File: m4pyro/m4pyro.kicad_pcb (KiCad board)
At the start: 2 copper layers, 140 parts, among them IC1 STM32F405RxTx, IC10 LTC4151, IC2 TPS62133, IC3 MCP2562, IC4 TPS62153, IC5 ADP2389, IC6 LTC4151, IC7 ADP2389, IC8 LTC4151, IC9 ADP2389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

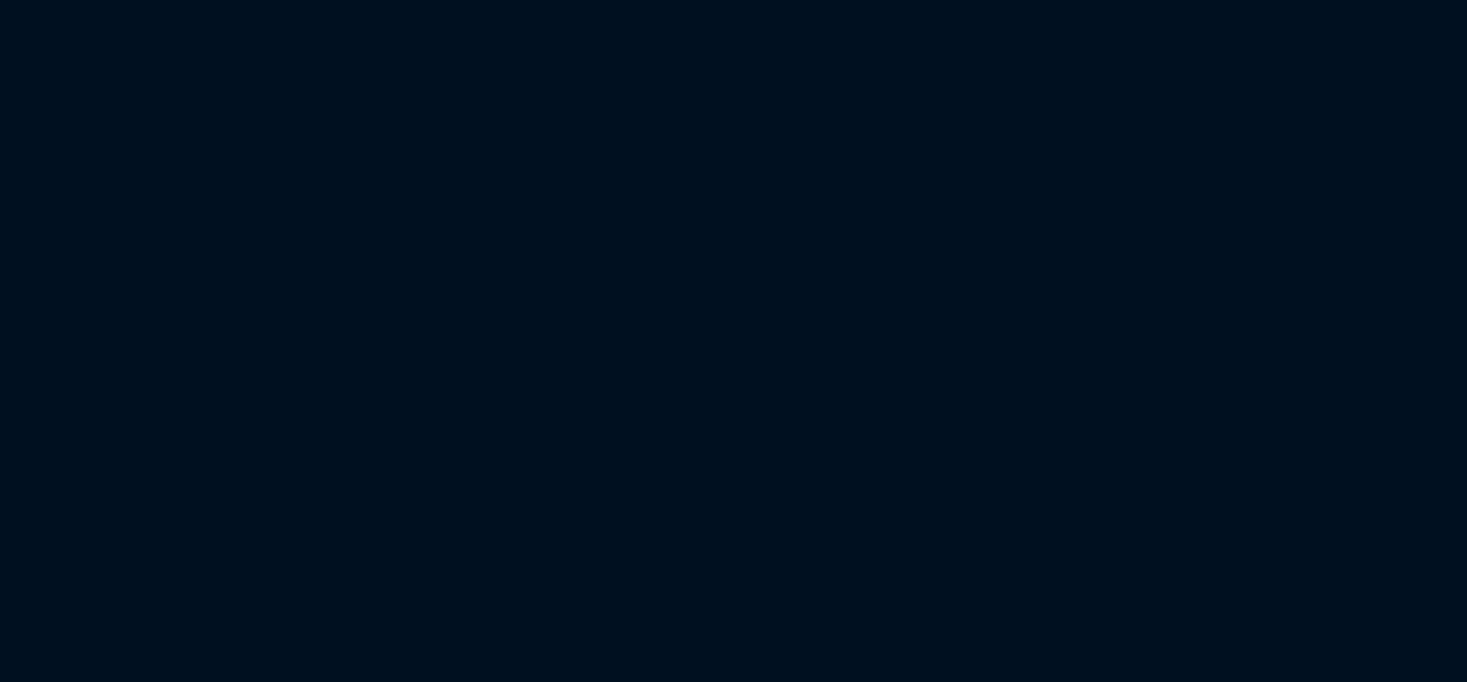
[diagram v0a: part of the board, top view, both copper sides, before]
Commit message: pyro schematic almost done
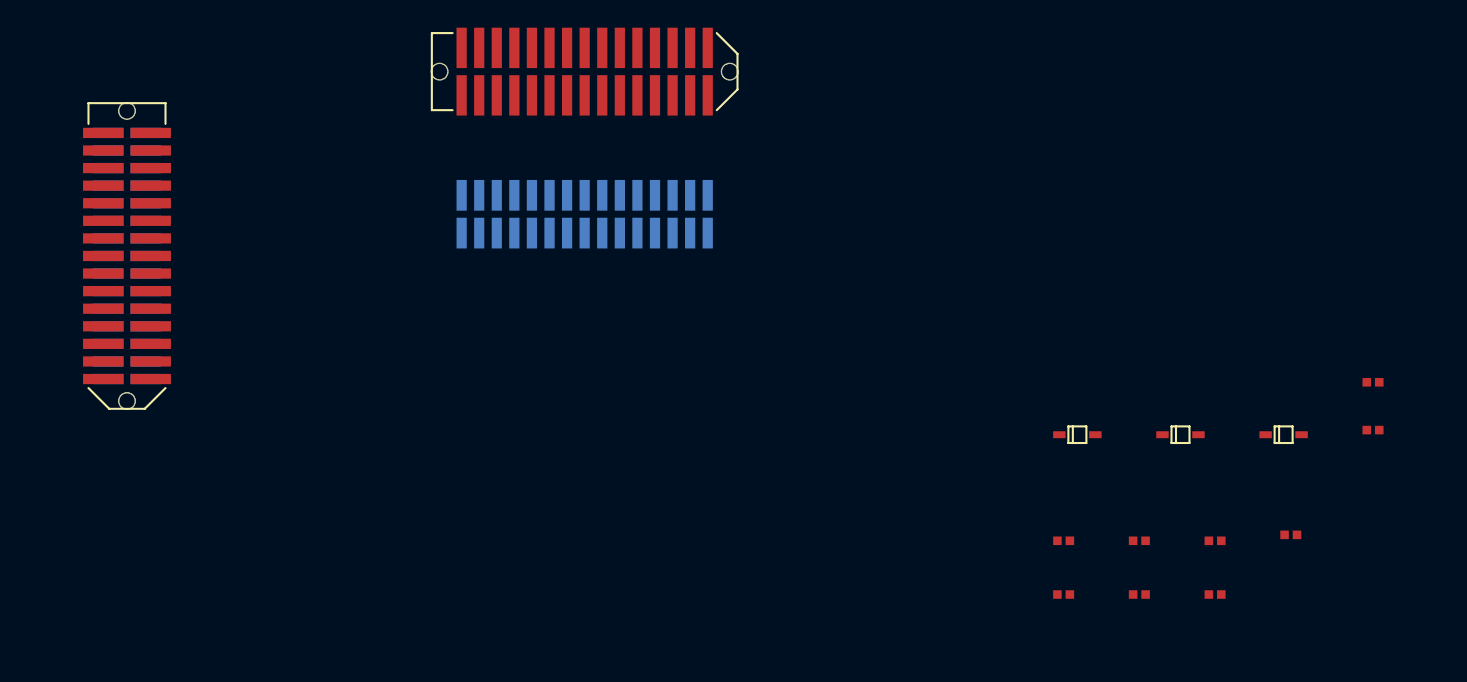
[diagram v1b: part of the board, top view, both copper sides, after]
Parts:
- added C48: 100n, agg:0402, F.Cu at (183.7, 46.2)
- added C49: 100n, agg:0402, F.Cu at (189.1, 46.2)
- added C50: 100n, agg:0402, F.Cu at (194.6, 46.2)
- added D12: PMEG3005AEA, agg:SOD-323, F.Cu at (184.7, 38.5)
- added D13: PMEG3005AEA, agg:SOD-323, F.Cu at (192.1, 38.5)
- added D14: PMEG3005AEA, agg:SOD-323, F.Cu at (199.6, 38.5)
- added J1: WEST TOP, agg:TFML-115-02-L-D-LC, F.Cu at (116.0, 25.6)
- added J2: WEST BOT, agg:SFML-115-02-L-D, B.Cu at (116.0, 25.6)
- added J3: EAST TOP, agg:TFML-115-02-L-D-LC, F.Cu at (149.1, 12.3)
- added J4: EAST BOT, agg:SFML-115-02-L-D, B.Cu at (149.1, 22.6)
- added R58: 1k, agg:0402, F.Cu at (183.7, 50.1)
- added R59: 1k, agg:0402, F.Cu at (189.1, 50.1)
- added R60: 1k, agg:0402, F.Cu at (206.0, 34.7)
- added R61: 10k, agg:0402, F.Cu at (194.6, 50.1)
- added R62: 10k, agg:0402, F.Cu at (206.0, 38.2)
- added R63: 10k, agg:0402, F.Cu at (200.1, 45.7)
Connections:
- IC1 pad 50: (no net) -> /JTDI
- IC1 pad 55: (no net) -> /JTDO
- IC3 pad 6: (no net) -> /CAN-
- IC3 pad 7: (no net) -> /CAN+

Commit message: started pyro pcb
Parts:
- added X2: HOLE, agg:M3_MOUNT, F.Cu at (57.5, 84.0)
- added X3: HOLE, agg:M3_MOUNT, F.Cu at (57.5, 116.0)
- added X4: HOLE, agg:M3_MOUNT, F.Cu at (142.5, 84.0)
- added X5: HOLE, agg:M3_MOUNT, F.Cu at (142.5, 116.0)
- L3, L4, L5: footprint agg:WE-HCC-1090 -> agg:WE-HCC-1090
- moved L4 204.8 mm to (273.5, 92.0), turned to 0 degrees
- moved IC9 181.4 mm to (232.9, 24.7)
- moved L5 160.4 mm to (274.4, 102.9)
- moved L3 154.6 mm to (188.6, 9.70)
- moved IC5 144.5 mm to (184.4, 19.2)
- moved IC7 139.3 mm to (200.0, 62.8)
- moved R44 131.9 mm to (167.2, 14.1)
- moved C30 117.6 mm to (193.0, 21.1)
- moved R46 115.9 mm to (193.2, 25.8)
- moved C40 109.4 mm to (185.5, 26.3)
- moved R45 104.3 mm to (193.2, 24.2)
- moved C27 97.4 mm to (191.6, 17.2)
- moved Q5 97.0 mm to (178.4, 76.4)
- moved R53 94.9 mm to (233.3, 68.8)
- moved J1 94.6 mm to (57.5, 100.0)
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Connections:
- IC1 pad 10: (no net) -> /V3_CONT
- IC1 pad 14: /LED_RED -> /CH1_CONT
- IC1 pad 15: /LED_YLW -> /CH2_CONT
- IC1 pad 16: /LED_GRN -> /CH3_CONT
- IC1 pad 17: (no net) -> /CH4_CONT
- IC1 pad 2: (no net) -> /LED_RED
- IC1 pad 20: /SI_DIV -> /CH5_CONT
- IC1 pad 21: /BUS_DIV -> /CH6_CONT
- IC1 pad 22: (no net) -> /CH7_CONT
- IC1 pad 23: (no net) -> /CH8_CONT
- IC1 pad 26: (no net) -> /SI_DIV
- IC1 pad 27: (no net) -> /BUS_DIV
- IC1 pad 29: (no net) -> /SCL
- IC1 pad 3: (no net) -> /LED_YLW
- IC1 pad 30: (no net) -> /SDA
- IC1 pad 4: (no net) -> /LED_GRN
- IC1 pad 42: (no net) -> /UART_TX
- IC1 pad 43: /1A_EN -> /UART_RX
- IC1 pad 44: (no net) -> /1A_EN
- IC1 pad 51: (no net) -> /V1_FIRE
- IC1 pad 52: (no net) -> /V2_FIRE
- IC1 pad 53: (no net) -> /V3_FIRE
- IC1 pad 8: (no net) -> /V1_CONT
- IC1 pad 9: (no net) -> /V2_CONT
- IC5 pad 28: (no net) -> /V1_FIRE
- IC7 pad 28: (no net) -> /V2_FIRE
- IC9 pad 28: (no net) -> /V3_FIRE
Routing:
- net GND: track 0.00 -> 101.9 mm, vias 0 -> 16
- net 3v3: track 0.00 -> 16.3 mm, vias 0 -> 2
- net /UART_RX: track 0.00 -> 3.32 mm, vias 0 -> 1
- net /3v3_AUX1: track 0.00 -> 3.32 mm, vias 0 -> 1
- net /RSVD8: track 0.00 -> 3.32 mm, vias 0 -> 1
- net /5v_RADIO: track 0.00 -> 3.32 mm, vias 0 -> 1
- net /RSVD4: track 0.00 -> 3.30 mm, vias 0 -> 1
- net /5v_CAN: track 0.00 -> 3.30 mm, vias 0 -> 1
- net /RSVD11: track 0.00 -> 3.30 mm, vias 0 -> 1
- net /PYRO6: track 0.00 -> 3.30 mm, vias 0 -> 1
- net /PYRO5: track 0.00 -> 3.30 mm, vias 0 -> 1
- net /RSVD12: track 0.00 -> 3.28 mm, vias 0 -> 1
- net /PYRO4: track 0.00 -> 3.28 mm, vias 0 -> 1
- net /PYRO3: track 0.00 -> 3.28 mm, vias 0 -> 1
- net /5v_CAM2: track 0.00 -> 3.28 mm, vias 0 -> 1
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- removed copper zone on F.Cu, net Net-(C37-Pad2)
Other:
- board outline added: 100 x 50 mm
- net class Default: clearance 0.2 -> 0.15; trace_width 0.25 -> 0.2; via_dia 0.8 -> 0.6
- rule trace_clearance: 0.2 -> 0.15
- rule via_min_size: 0.4 -> 0.6

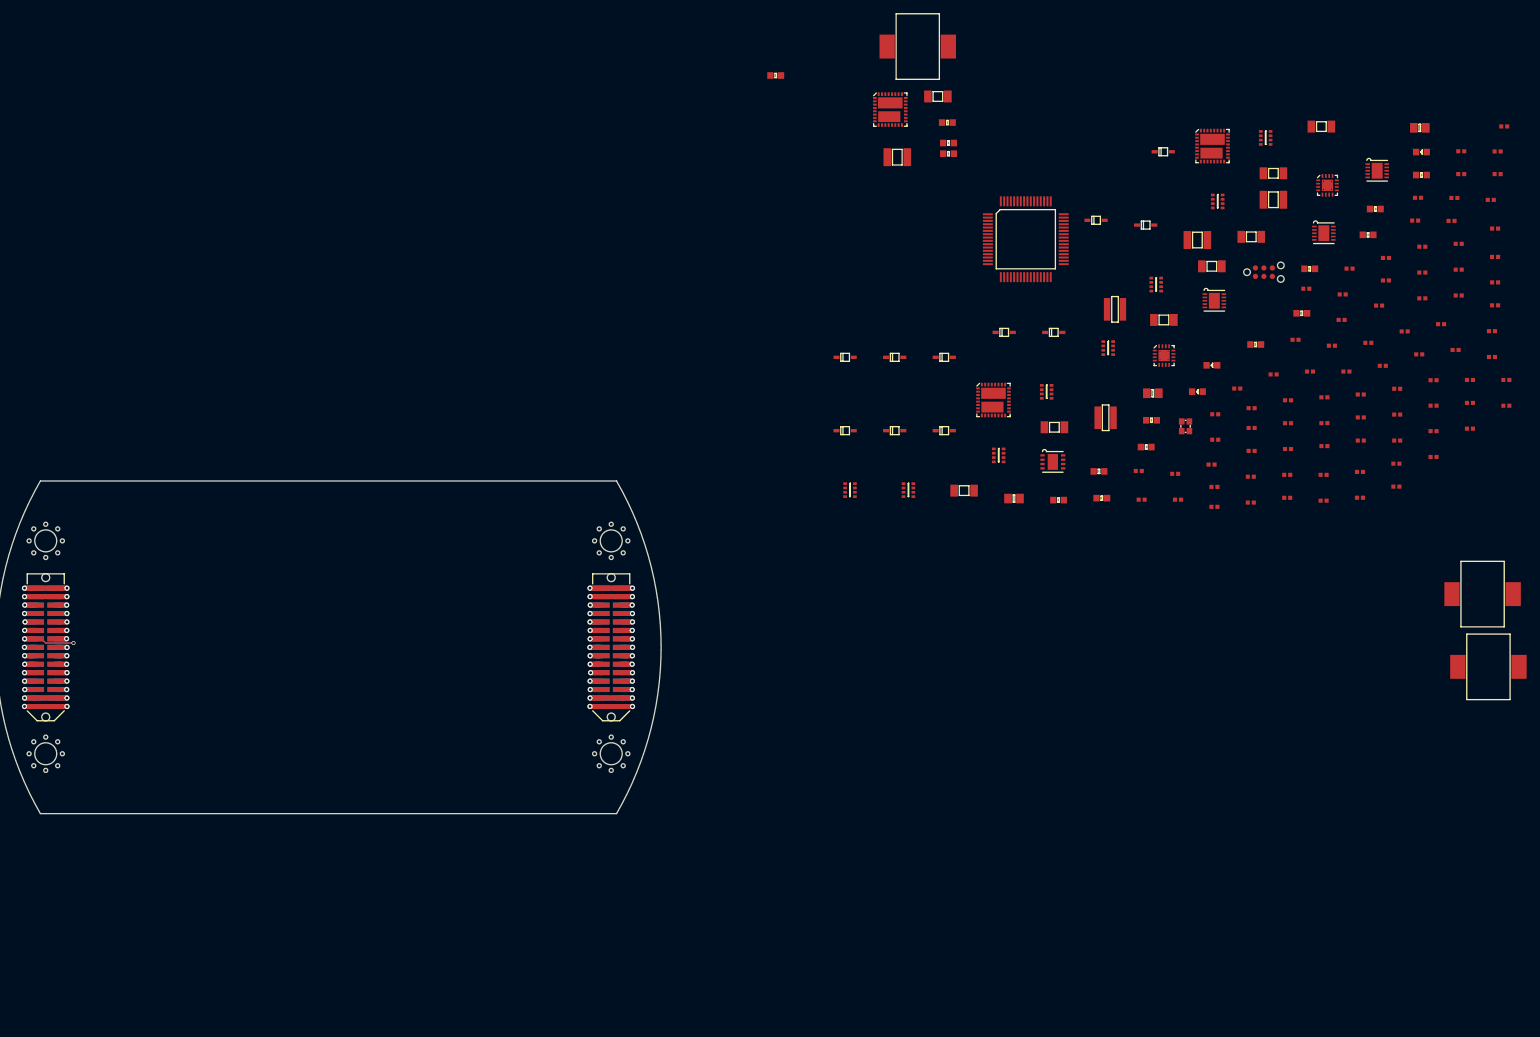
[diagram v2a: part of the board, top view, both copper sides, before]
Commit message: laying out pyro valve components
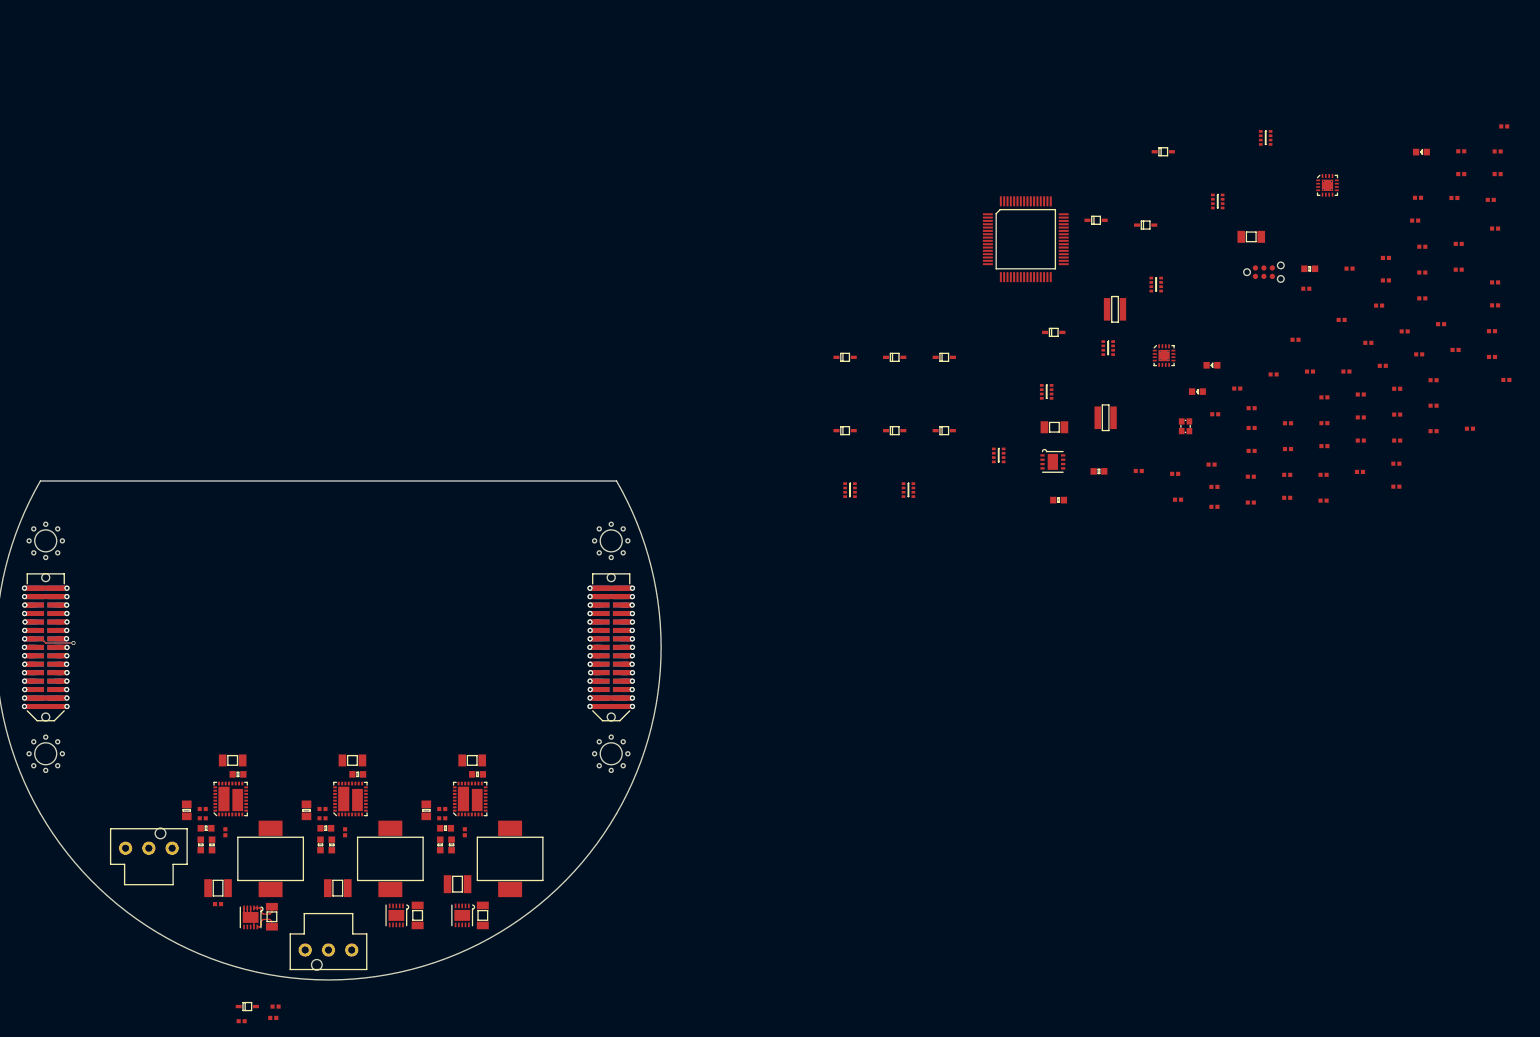
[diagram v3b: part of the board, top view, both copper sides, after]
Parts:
- added J5: SUPPLY, agg:ultra-fit-01x03, F.Cu at (73.0, 130.2)
- added J6: VALVES, agg:ultra-fit-01x03, F.Cu at (100.0, 145.5)
- moved R43 211.2 mm to (81.1, 124.3)
- moved C29 207.6 mm to (83.4, 138.6)
- moved C28 202.2 mm to (84.5, 127.8), turned to 90 degrees
- moved R61 201.2 mm to (92.0, 154.0)
- moved C39 196.3 mm to (96.7, 124.5), turned to 270 degrees
- moved C31 192.8 mm to (81.1, 125.7)
- moved C48 192.8 mm to (87.0, 156.2)
- moved C33 189.4 mm to (83.4, 136.2)
- moved C35 182.2 mm to (102.5, 127.8), turned to 90 degrees
- moved R49 180.3 mm to (99.6, 127.2), turned to 180 degrees
- moved R58 178.6 mm to (91.7, 155.7)
- moved IC10 177.3 mm to (120.1, 140.3), turned to 270 degrees
- moved R54 176.5 mm to (117.6, 127.2), turned to 180 degrees
- moved C45 176.3 mm to (117.1, 125.7)
- moved IC8 173.1 mm to (110.2, 140.3), turned to 270 degrees
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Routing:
- net GND: track 101.9 -> 108.6 mm
- net /V_1_SUPPLY: track 0.00 -> 4.24 mm
- net /VALVE_1: track 0.00 -> 3.94 mm
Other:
- board size 100 x 50 mm -> 100 x 75 mm

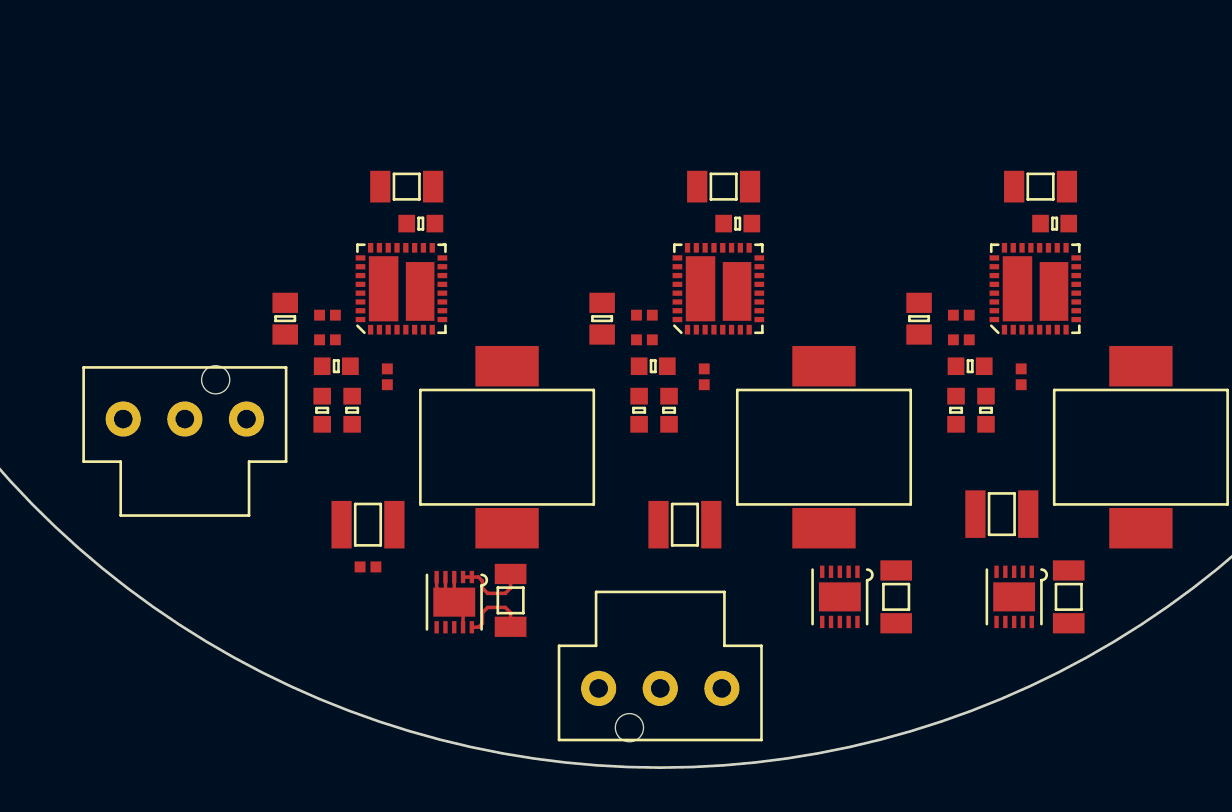
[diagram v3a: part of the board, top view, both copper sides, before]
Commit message: added pcb template
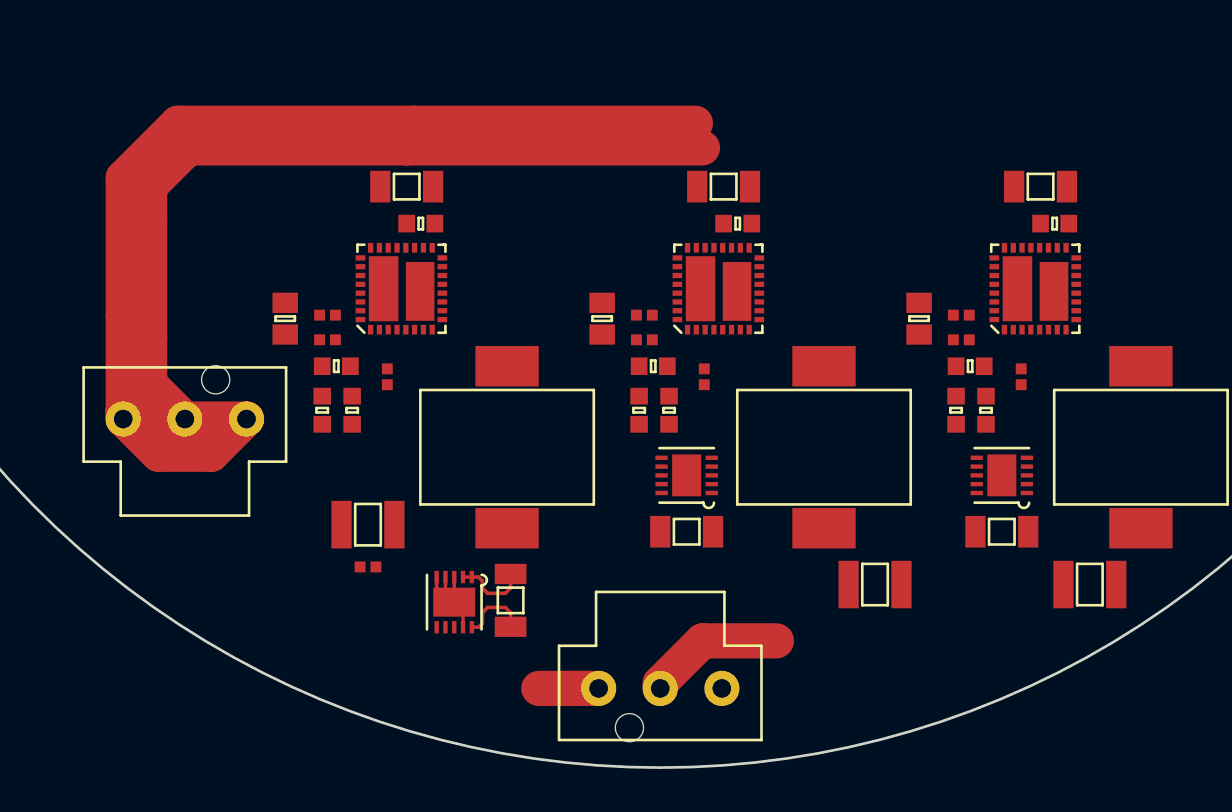
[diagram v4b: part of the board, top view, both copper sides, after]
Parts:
- moved R52 12.5 mm to (101.5, 136.6), turned to 0 degrees
- moved C40 11.3 mm to (112.2, 139.6), turned to 180 degrees
- moved IC8 11.1 mm to (101.5, 133.4), turned to 180 degrees
- moved IC10 6.94 mm to (119.4, 133.4), turned to 180 degrees
- moved C47 6.40 mm to (124.4, 139.6), turned to 180 degrees
- moved R57 5.30 mm to (119.4, 136.6), turned to 0 degrees
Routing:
- net /PYRO_SI: track 0.00 -> 112.1 mm
- net /VALVE_2: track 0.00 -> 7.89 mm
- net /VALVE_1: track 3.94 -> 7.34 mm

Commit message: put down high current tracks
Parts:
- moved C49 227.9 mm to (88.8, 164.6)
- moved R63 219.9 mm to (88.2, 172.6)
- moved R59 218.2 mm to (88.2, 160.8)
- moved C50 210.7 mm to (88.8, 174.3)
- moved R60 198.2 mm to (88.5, 170.8)
- moved R62 192.7 mm to (88.8, 163.3)
- moved C36 175.2 mm to (102.5, 130.2), turned to 270 degrees
- moved C43 169.9 mm to (120.5, 130.2), turned to 270 degrees
- moved D14 158.6 mm to (88.8, 176.3)
- moved D13 135.0 mm to (88.7, 162.0)
- moved C47 2.75 mm to (121.8, 140.5), turned to 90 degrees
- moved C29 2.51 mm to (85.7, 139.6), turned to 90 degrees
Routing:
- net /PYRO_SI: track 112.1 -> 198.3 mm
- net /VALVE_3: track 0.00 -> 38.6 mm
- net /V_2_SUPPLY: track 0.00 -> 22.8 mm
- net /V_1_SUPPLY: track 4.24 -> 25.7 mm
- net /V_3_SUPPLY: track 0.00 -> 18.6 mm
- net Net-(IC5-Pad3): track 0.06 -> 6.38 mm
- net Net-(IC9-Pad3): track 0.00 -> 6.32 mm
- net Net-(IC7-Pad3): track 0.00 -> 6.32 mm
- net /VALVE_2: track 7.89 -> 12.8 mm
- net /VALVE_1: track 7.34 -> 11.7 mm
- net Net-(C39-Pad2): track 0.00 -> 3.43 mm
- net Net-(C46-Pad2): track 0.00 -> 3.37 mm
- net Net-(IC7-Pad2): track 0.00 -> 3.29 mm
- net Net-(C32-Pad2): track 0.00 -> 3.26 mm
- net Net-(IC9-Pad2): track 0.00 -> 3.23 mm
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- added copper zone on F.Cu, net /PYRO_SI
- added copper zone on F.Cu, net /VALVE_1
- added copper zone on F.Cu, net /VALVE_2
- added copper zone on F.Cu, net /VALVE_3
- added copper zone on F.Cu, net /V_1_SUPPLY
- added copper zone on F.Cu, net /V_2_SUPPLY
- added copper zone on F.Cu, net /V_3_SUPPLY
- added copper zone on B.Cu, net GND
- added copper zone on F.Cu, net GND
- added copper zone on F.Cu, net Net-(C30-Pad2)
- added copper zone on F.Cu, net Net-(C37-Pad2)
- added copper zone on F.Cu, net Net-(C44-Pad2)
